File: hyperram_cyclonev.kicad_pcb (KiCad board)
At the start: 2 copper layers, 90.1 x 89.7 mm, 57 parts, among them IC1 AP63205WU, IC2 TXB0108PWR, IC3 S26KL128SDABHI020, IC4 W25Q32JVSSIQ_TR, IC5 S27KL0641DABHI020, J1 ASP-122952-01, J2 HDMI_A, J3 Conn_02x10_Odd_Even, J4 Conn_02x06_Odd_Even, J5 Conn_02x06_Top_Bottom, J6 Conn_02x06_Top_Bottom, J7 Conn_02x06_Top_Bottom, Q1 BSS138, Q2 BSS138

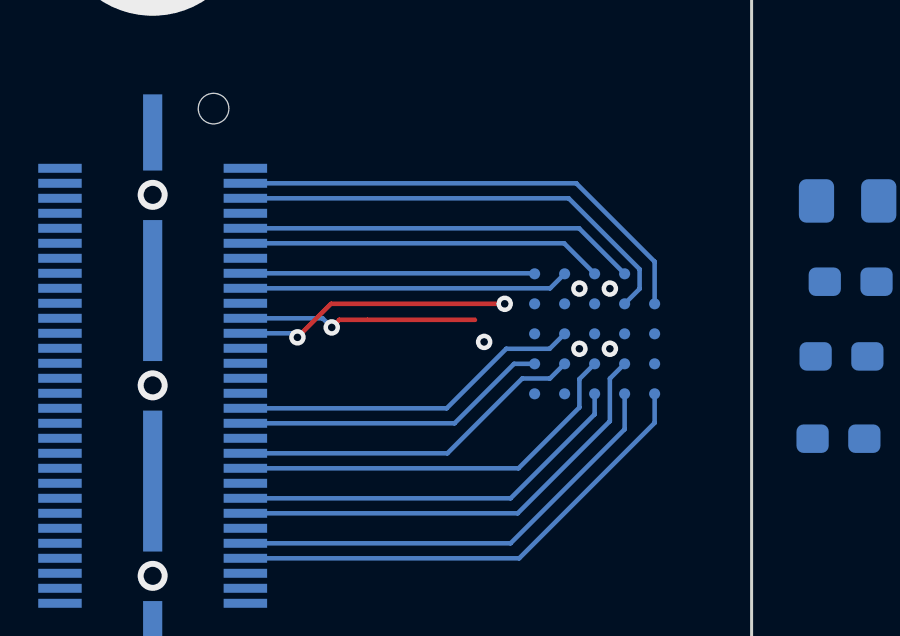
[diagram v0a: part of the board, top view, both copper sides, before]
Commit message: Fixed differential pairs designators for HyperRAM clk and psc and HDMI clk and data.
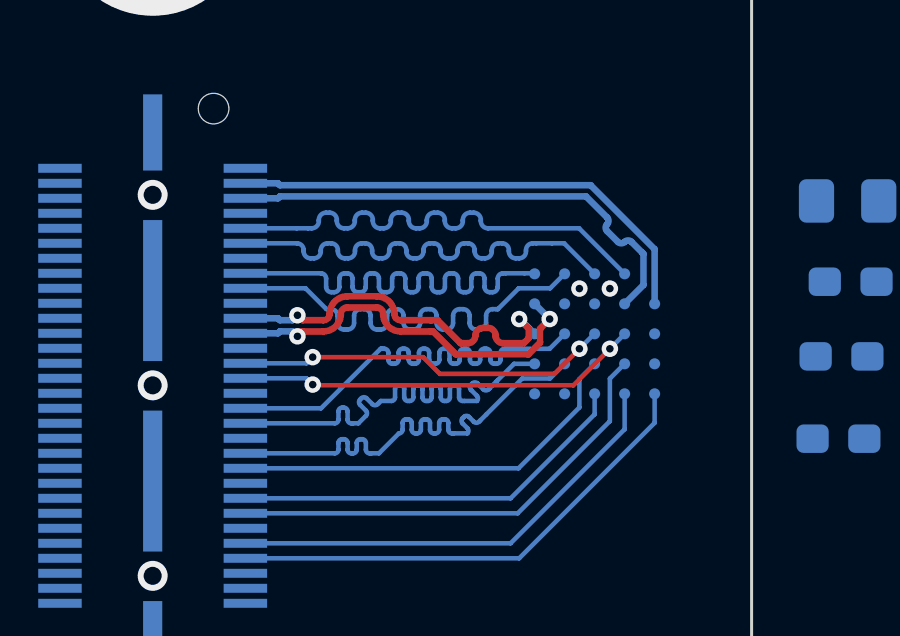
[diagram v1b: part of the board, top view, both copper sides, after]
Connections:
- net /hdmi_clkn renamed /hdmi_clk-
- net /hdmi_clkp renamed /hdmi_clk+
- net /hdmi_d0n renamed /hdmi_d0-
- net /hdmi_d0p renamed /hdmi_d0+
- net /hdmi_d1n renamed /hdmi_d1-
- net /hdmi_d1p renamed /hdmi_d1+
- net /hdmi_d2n renamed /hdmi_d2-
- net /hdmi_d2p renamed /hdmi_d2+
- net /hf_psc renamed /hf_psc+
- net /hf_pscn renamed /hf_psc-
- net /hr1_clkn renamed /hr1_clk-
- net /hr1_clkp renamed /hr1_clk+
- net /hr2_clkn renamed /hr2_clk-
- net /hr2_clkp renamed /hr2_clk+
- net /pmod3_io0n renamed /pmod3_io0
- net /pmod3_io0p renamed /pmod3_io4
- net /pmod3_io1n renamed /pmod3_io1
- net /pmod3_io1p renamed /pmod3_io5
- net /pmod3_io2n renamed /pmod3_io2
- net /pmod3_io2p renamed /pmod3_io6
- net /pmod3_io3n renamed /pmod3_io3
- net /pmod3_io3p renamed /pmod3_io7
- net /pmod3_io4n renamed /pmod3_io8
- net /pmod3_io4p renamed /pmod3_io12
- net /pmod3_io5n renamed /pmod3_io9
- net /pmod3_io5p renamed /pmod3_io13
- net /pmod3_io6n renamed /pmod3_io10
- net /pmod3_io6p renamed /pmod3_io14
- net /pmod3_io7n renamed /pmod3_io11
- net /pmod3_io7p renamed /pmod3_io15
- net /xhdmi_clkn renamed /xhdmi_clk-
- net /xhdmi_clkp renamed /xhdmi_clk+
- net /xhdmi_d0n renamed /xhdmi_d0-
- net /xhdmi_d0p renamed /xhdmi_d0+
- net /xhdmi_d1n renamed /xhdmi_d1-
- net /xhdmi_d1p renamed /xhdmi_d1+
- net /xhdmi_d2n renamed /xhdmi_d2-
- net /xhdmi_d2p renamed /xhdmi_d2+
- J1 pad 131: /hr2_rwds -> /hf_csn
- J1 pad 133: /hf_csn -> /hr2_rwds
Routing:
- net /hf_csn: track 0.00 -> 13.5 mm, vias 1 -> 2
- net /hr2_rwds: track 0.00 -> 12.5 mm, vias 1 -> 2
- net /hf_intn: track 9.65 -> 16.2 mm
- net /hr2_dq4: track 10.5 -> 16.1 mm
- net /hr2_rstn: track 10.8 -> 16.2 mm
- net /hf_psc-: track 7.89 -> 12.9 mm
- net /hr2_dq2: track 11.7 -> 16.1 mm
- net /hr2_dq3: track 11.9 -> 16.1 mm
- net /hr2_csn: track 12.1 -> 16.1 mm
- net /hf_psc+: track 9.16 -> 12.9 mm
- net /hf_rston: track 13.3 -> 16.2 mm
- net /hr2_clk+: track 15.5 -> 16.4 mm

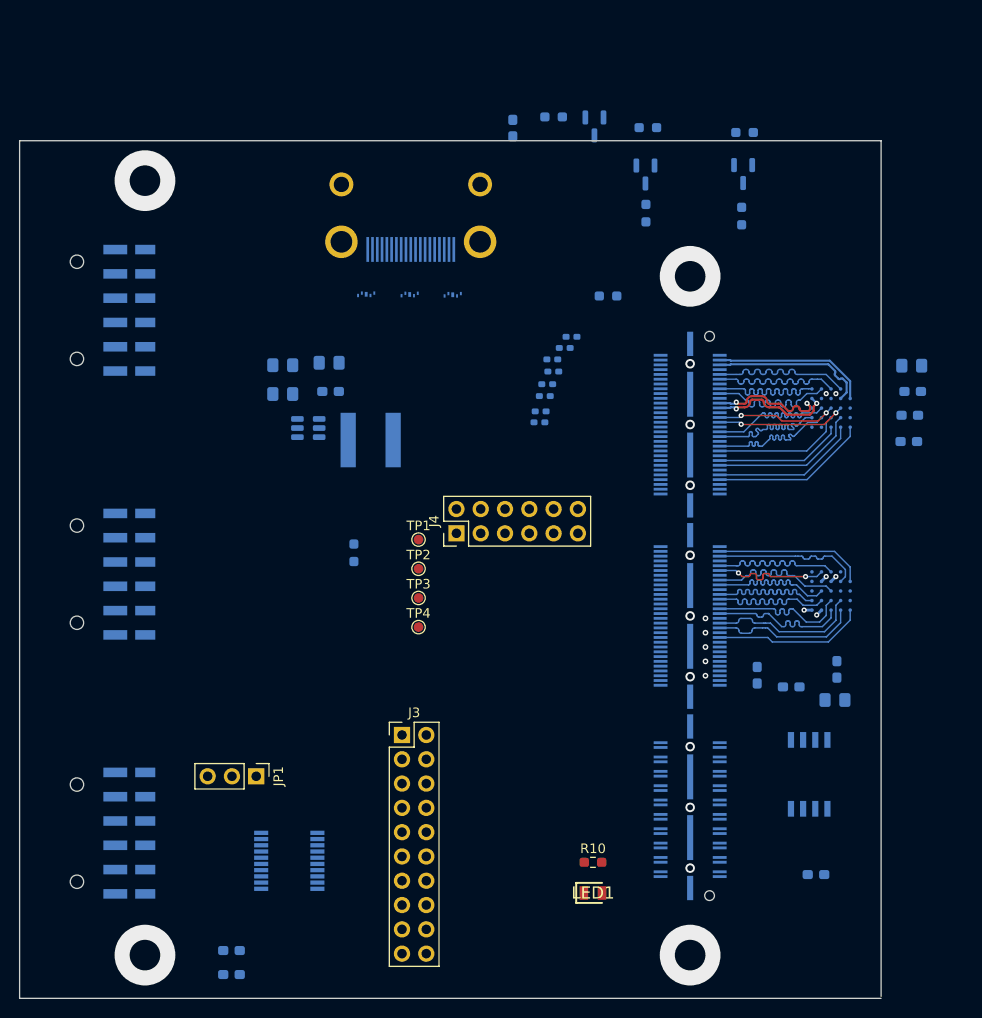
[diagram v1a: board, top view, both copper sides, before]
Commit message: Decreased board area. Fixed HyperRAM clk diff pair routing. First try for HDMI diff pair routing.
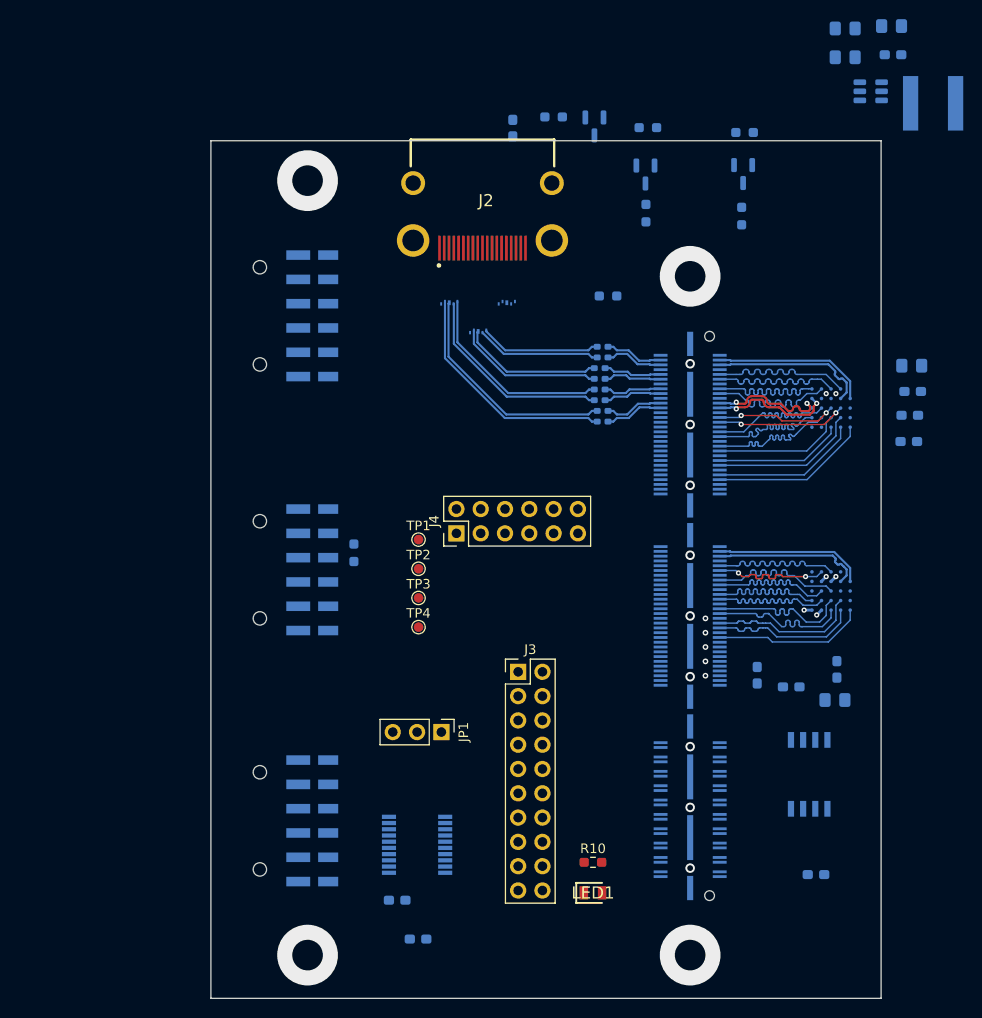
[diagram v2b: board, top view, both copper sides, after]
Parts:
- J2: moved to F.Cu
- moved C3 68.5 mm to (243.7, 54.5)
- moved C5 68.5 mm to (243.6, 51.5)
- moved C2 68.5 mm to (238.7, 51.8)
- moved C4 68.5 mm to (238.7, 54.8)
- moved IC1 68.5 mm to (241.4, 58.3)
- moved L1 68.5 mm to (247.9, 59.6)
- moved JP1 19.9 mm to (196.5, 125.3)
- moved C7 19.9 mm to (194.1, 147.0)
- moved J5 19.2 mm to (177.6, 134.6)
- moved J7 19.1 mm to (177.6, 81.8)
- moved J6 19.1 mm to (177.6, 108.4)
- moved C6 18.1 mm to (191.9, 142.9)
- moved D2 14.7 mm to (203.3, 80.4), turned to 90 degrees
- moved J3 13.8 mm to (204.5, 119.0)
- moved IC2 13.5 mm to (194.0, 137.1)
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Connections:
- C19 pad 1: /hdmi_d0+ -> /hdmi_d2+
- C19 pad 2: /xhdmi_d0+ -> /xhdmi_d2+
- C20 pad 1: /hdmi_d0- -> /hdmi_d2-
- C20 pad 2: /xhdmi_d0- -> /xhdmi_d2-
- C23 pad 1: /hdmi_d2+ -> /hdmi_d0+
- C23 pad 2: /xhdmi_d2+ -> /xhdmi_d0+
- C24 pad 1: /hdmi_d2- -> /hdmi_d0-
- C24 pad 2: /xhdmi_d2- -> /xhdmi_d0-
- J1 pad 138: /hdmi_d0+ -> /hdmi_d2+
- J1 pad 140: /hdmi_d0- -> /hdmi_d2-
- J1 pad 150: /hdmi_d2+ -> /hdmi_d0+
- J1 pad 152: /hdmi_d2- -> /hdmi_d0-
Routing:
- net /xhdmi_d2+: track 0.00 -> 24.6 mm
- net /xhdmi_d2-: track 0.00 -> 23.9 mm
- net /xhdmi_d1+: track 0.00 -> 21.3 mm
- net /xhdmi_d1-: track 0.00 -> 20.9 mm
- net /xhdmi_d0+: track 0.00 -> 15.5 mm
- net /xhdmi_d0-: track 0.00 -> 14.8 mm
- net /xhdmi_clk+: track 0.00 -> 13.1 mm
- net /xhdmi_clk-: track 0.00 -> 12.7 mm
- net /hdmi_d1+: track 0.00 -> 6.14 mm
- net /hdmi_d1-: track 0.00 -> 6.14 mm
- net /hdmi_d2-: track 0.00 -> 6.14 mm
- net /hdmi_d2+: track 0.00 -> 6.14 mm
- net /hdmi_d0-: track 0.00 -> 6.13 mm
- net /hdmi_d0+: track 0.00 -> 6.13 mm
- net /hdmi_clk-: track 0.00 -> 6.13 mm
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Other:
- board size 90.1 x 89.7 mm -> 70.1 x 89.7 mm

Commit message: Routed almost all single ended signals, except HDMI and power
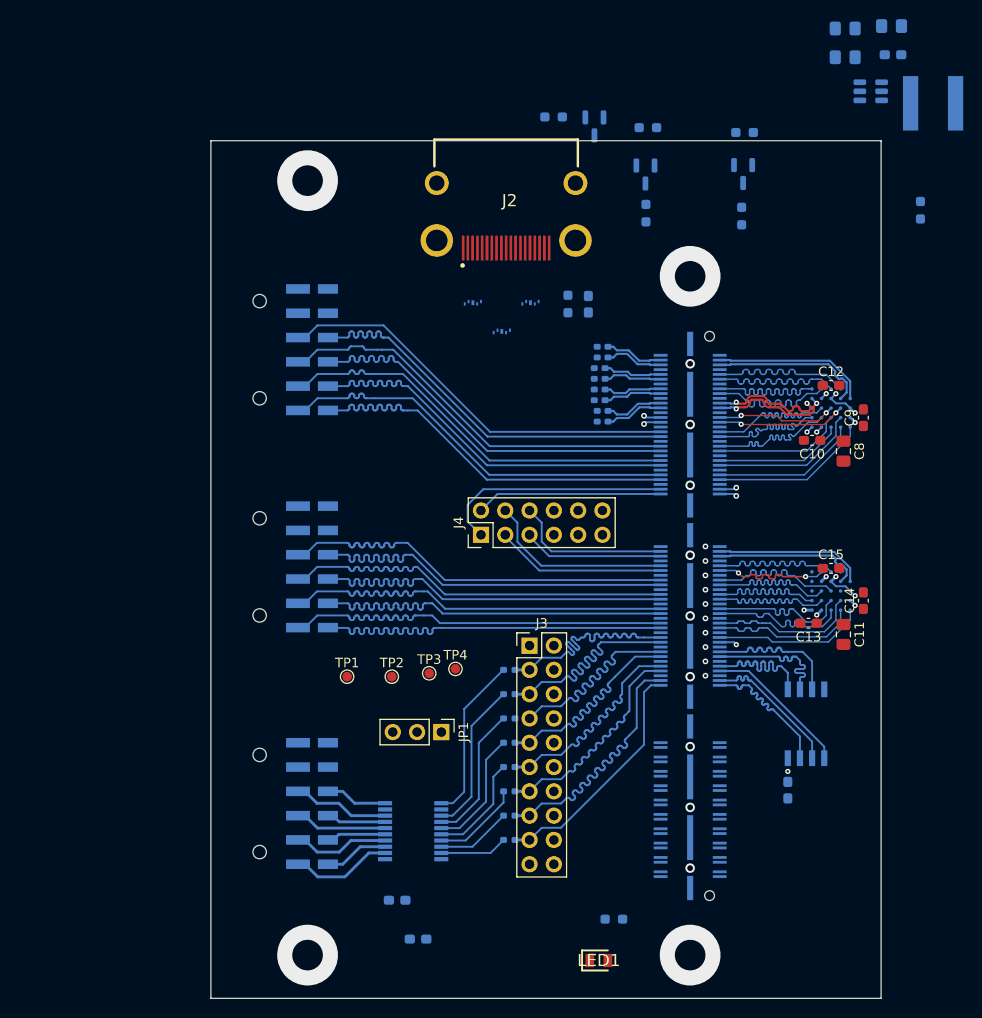
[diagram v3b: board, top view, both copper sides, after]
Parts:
- added R11: 0, Resistor_SMD:R_0402_1005Metric_Pad0.72x0.64mm_HandSolder, B.Cu at (203.6, 131.5)
- added R12: 0, Resistor_SMD:R_0402_1005Metric_Pad0.72x0.64mm_HandSolder, B.Cu at (203.6, 129.0)
- added R13: 0, Resistor_SMD:R_0402_1005Metric_Pad0.72x0.64mm_HandSolder, B.Cu at (203.6, 126.4)
- added R14: 0, Resistor_SMD:R_0402_1005Metric_Pad0.72x0.64mm_HandSolder, B.Cu at (203.6, 123.9)
- added R15: 0, Resistor_SMD:R_0402_1005Metric_Pad0.72x0.64mm_HandSolder, B.Cu at (203.6, 121.4)
- added R16: 0, Resistor_SMD:R_0402_1005Metric_Pad0.72x0.64mm_HandSolder, B.Cu at (203.6, 118.8)
- added R8: 0, Resistor_SMD:R_0402_1005Metric_Pad0.72x0.64mm_HandSolder, B.Cu at (203.6, 136.6)
- added R9: 0, Resistor_SMD:R_0402_1005Metric_Pad0.72x0.64mm_HandSolder, B.Cu at (203.6, 134.1)
- C10, C11, C12, C13, C14, C15, C8, C9: moved to F.Cu
- R10: moved to B.Cu
- moved R7 69.2 mm to (246.6, 70.8)
- moved C1 20.0 mm to (211.9, 80.6), turned to -90 degrees
- moved TP1 16.2 mm to (186.6, 119.5)
- moved C15 13.6 mm to (237.2, 108.2), turned to 0 degrees
- moved TP2 11.6 mm to (191.3, 119.5)
- moved C8 11.4 mm to (238.5, 96.0), turned to -90 degrees
- moved C10 10.5 mm to (235.3, 94.8)
- moved C12 10.0 mm to (237.2, 89.1), turned to 0 degrees
- moved C16 9.31 mm to (232.7, 131.4), turned to -90 degrees
- moved TP3 7.95 mm to (195.2, 119.2)
- moved C14 7.70 mm to (240.6, 111.6)
- moved LED1 7.09 mm to (213.0, 149.2)
- moved C11 6.92 mm to (238.5, 115.1), turned to -90 degrees
- moved C13 6.90 mm to (234.9, 113.9)
- moved R10 6.33 mm to (214.5, 144.9), turned to 180 degrees
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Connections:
- IC2 pad 1: /pmod5lv_io7 -> /pmod3t_io23
- IC2 pad 3: /pmod5lv_io6 -> /pmod3t_io22
- IC2 pad 4: /pmod5lv_io5 -> /pmod3t_io21
- IC2 pad 5: /pmod5lv_io4 -> /pmod3t_io20
- IC2 pad 6: /pmod5lv_io3 -> /pmod3t_io19
- IC2 pad 7: /pmod5lv_io2 -> /pmod3t_io18
- IC2 pad 8: /pmod5lv_io1 -> /pmod3t_io17
- IC2 pad 9: /pmod5lv_io0 -> /pmod3t_io16
- J1 pad 102: /debug_io2 -> /debug_io1
- J1 pad 104: /debug_io1 -> /debug_io0
- J1 pad 42: /pmod5lv_io0 -> /pmod3_io16
- J1 pad 44: /pmod5lv_io1 -> /pmod3_io17
- J1 pad 48: /pmod5lv_io2 -> /pmod3_io18
- J1 pad 50: /pmod5lv_io3 -> /pmod3_io19
- J1 pad 54: /pmod5lv_io4 -> /pmod3_io20
- J1 pad 56: /pmod5lv_io5 -> /pmod3_io21
- J1 pad 59: /debug_io7 -> /debug_io6
- J1 pad 60: /pmod5lv_io6 -> /pmod3_io22
- J1 pad 62: /pmod5lv_io7 -> /pmod3_io23
- J1 pad 90: /debug_io6 -> /debug_io2
- J1 pad 92: /debug_io5 -> /debug_io3
- J1 pad 98: /debug_io3 -> /debug_io5
- J3 pad 11: /pmod5lv_io3 -> /pmod3_io19
- J3 pad 13: /pmod5lv_io2 -> /pmod3_io18
- J3 pad 15: /pmod5lv_io1 -> /pmod3_io17
- J3 pad 17: /pmod5lv_io0 -> /pmod3_io16
- J3 pad 3: /pmod5lv_io7 -> /pmod3_io23
- J3 pad 5: /pmod5lv_io6 -> /pmod3_io22
- J3 pad 7: /pmod5lv_io5 -> /pmod3_io21
- J3 pad 9: /pmod5lv_io4 -> /pmod3_io20
- J4 pad 1: /cec -> /debug_io0
- J4 pad 8: /debug_io7 -> /cec
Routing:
- net /pmod3_io11: track 0.00 -> 43.0 mm
- net /pmod3_io10: track 0.00 -> 43.0 mm
- net /pmod3_io9: track 0.00 -> 43.0 mm
- net /pmod3_io8: track 0.00 -> 43.0 mm
- net /pmod3_io3: track 0.00 -> 42.9 mm
- net /pmod3_io2: track 0.00 -> 42.8 mm
- net /pmod3_io0: track 0.00 -> 42.8 mm
- net /pmod3_io1: track 0.00 -> 42.8 mm
- net /pmod3_io15: track 0.00 -> 42.8 mm
- net /pmod3_io6: track 0.00 -> 42.8 mm
- net /pmod3_io12: track 0.00 -> 42.8 mm
- net /pmod3_io14: track 0.00 -> 42.7 mm
- net /pmod3_io13: track 0.00 -> 42.7 mm
- net /pmod3_io5: track 0.00 -> 42.7 mm
- net /pmod3_io4: track 0.00 -> 42.7 mm
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
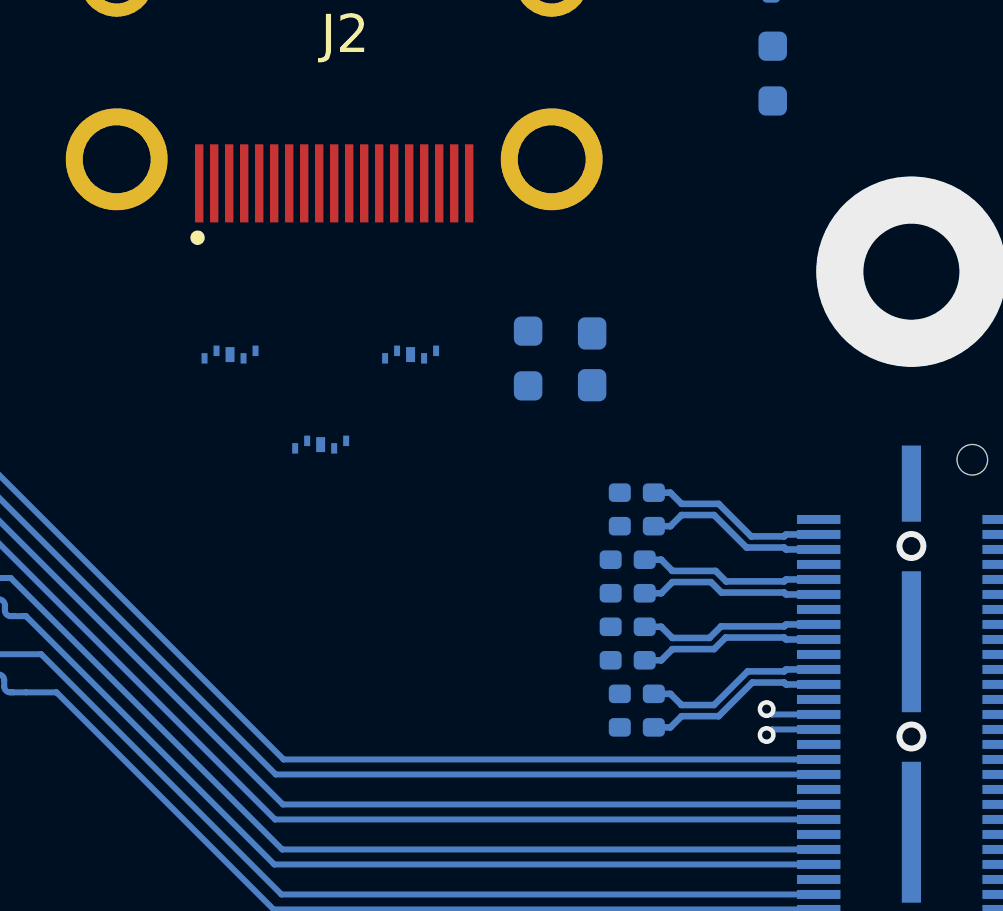
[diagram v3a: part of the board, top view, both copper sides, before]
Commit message: Routed HDMI differential signals for a first time, still with unmatched lenghts between pairs
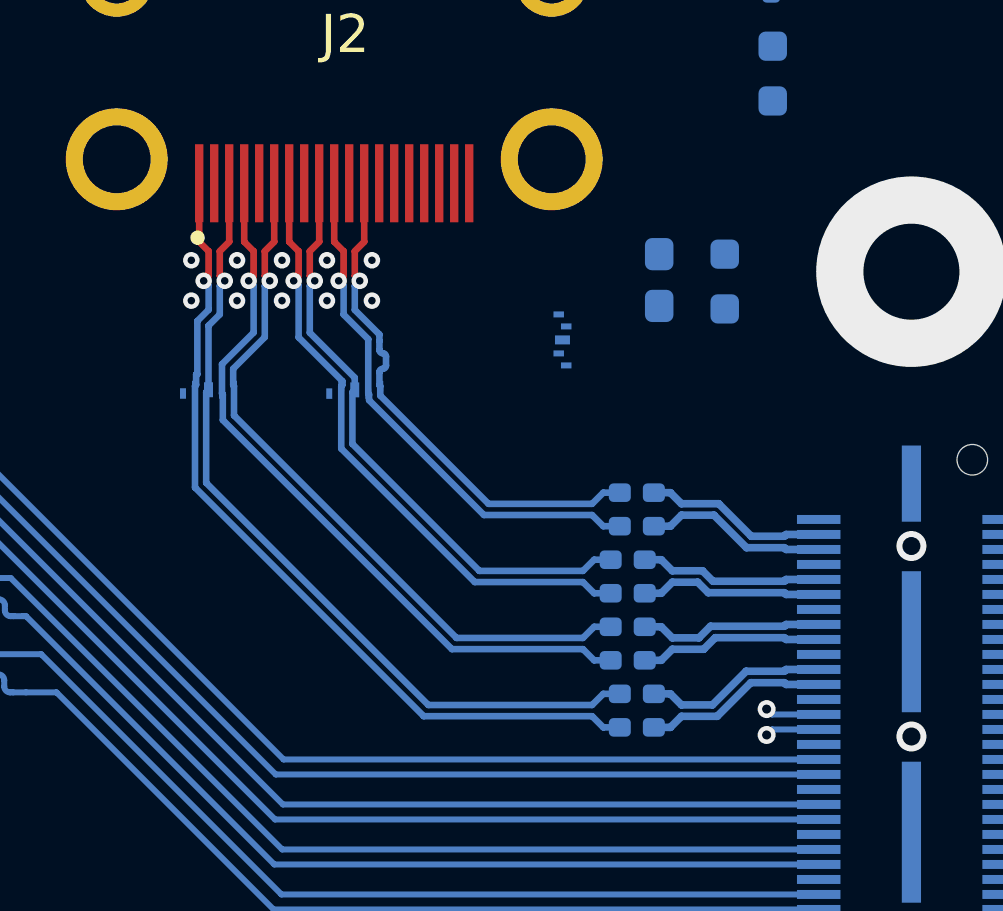
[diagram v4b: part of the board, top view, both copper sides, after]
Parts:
- moved R6 7.04 mm to (216.3, 78.0)
- moved D2 5.09 mm to (210.9, 79.9), turned to 180 degrees
- moved C1 3.46 mm to (214.1, 78.0)
- moved D1 2.15 mm to (203.9, 81.6)
- moved D4 1.37 mm to (199.1, 81.6)
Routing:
- net /xhdmi_d2+: track 0.00 -> 28.1 mm, vias 0 -> 1
- net /xhdmi_d2-: track 0.00 -> 27.4 mm, vias 0 -> 1
- net /xhdmi_d1+: track 0.00 -> 24.9 mm, vias 0 -> 1
- net /xhdmi_d1-: track 0.00 -> 24.2 mm, vias 0 -> 1
- net /xhdmi_d0+: track 0.00 -> 20.7 mm, vias 0 -> 1
- net /xhdmi_d0-: track 0.00 -> 20.1 mm, vias 0 -> 1
- net /xhdmi_clk+: track 0.00 -> 17.9 mm, vias 0 -> 1
- net /xhdmi_clk-: track 0.00 -> 17.6 mm, vias 0 -> 1
- net GND: vias 15 -> 25
